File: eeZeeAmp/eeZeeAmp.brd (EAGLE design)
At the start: 21.3 x 13.7 mm, 11 parts, among them IC1 LM386

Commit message: Minor updates, added gerbers, zip
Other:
- board text added: "10"
- board text added: "104"
- board text added: "106"
- board text added: "1K"
- board text added: "220uF"
- board text added: "503"
- board text added: "LM386"
- board text added: "VOL"

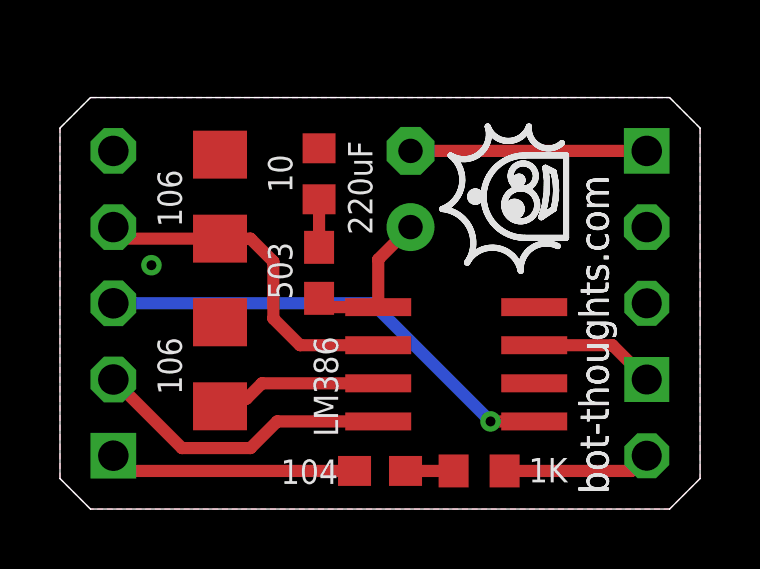
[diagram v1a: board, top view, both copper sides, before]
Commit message: Final version of silk
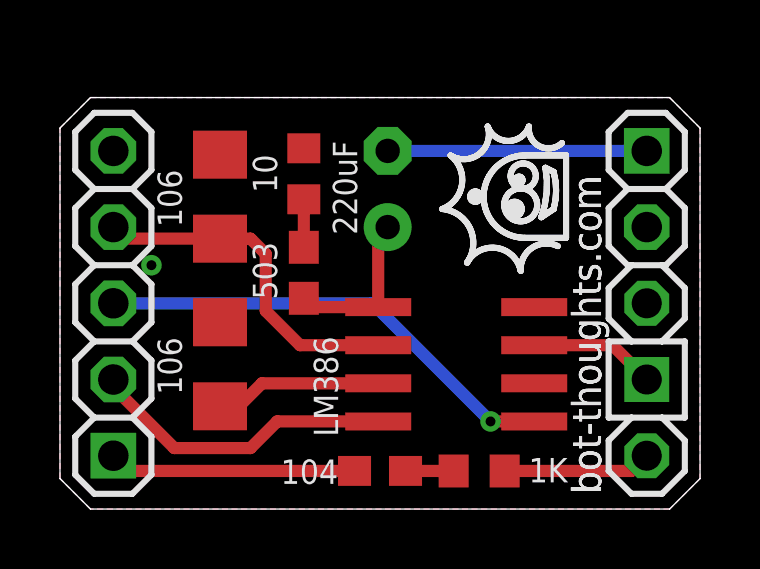
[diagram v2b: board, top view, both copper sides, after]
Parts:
- moved C1 0.76 mm to (10.9, 10.7)
- moved C3 0.51 mm to (8.13, 7.87)
- moved R1 0.51 mm to (8.13, 11.2)
- flipped JP1 to the top
- flipped JP2 to the top
- flipped R2 to the top
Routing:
- net SP+: track 7.87 -> 8.64 mm
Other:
- board text added: "1"
- board text added: "8"
- board text added: "GAIN"
- board text removed: "G1"
- board text removed: "G8"

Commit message: Fixed silk pin 1 on LM386, updated version #
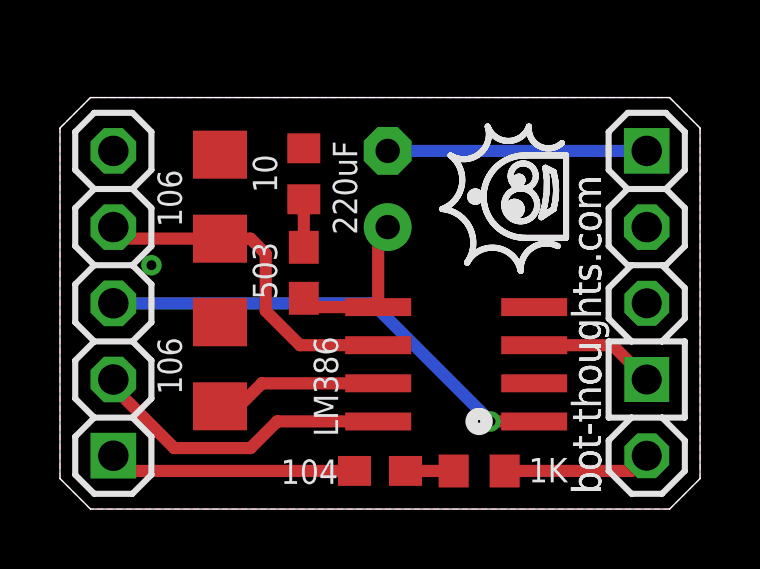
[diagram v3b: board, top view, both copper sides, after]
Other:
- board text added: "R0.2"
- board text removed: "R0.1"
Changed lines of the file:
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@@
 <layer number="49" name="Reference" color="7" fill="1" visible="no" active="yes"/>
 <layer number="50" name="dxf" color="7" fill="1" visible="no" active="no"/>
-<layer number="51" name="tDocu" color="7" fill="1" visible="no" active="yes"/>
+<layer number="51" name="tDocu" color="7" fill="1" visible="yes" active="yes"/>
 <layer number="52" name="bDocu" color="7" fill="1" visible="no" active="yes"/>
 <layer number="53" name="tPadExt" color="7" fill="1" visible="no" active="no"/>
@@
 <text x="18.288" y="8.89" size="1.27" layer="26" font="vector" ratio="12" rot="MR0">SP-</text>
 <text x="15.748" y="6.35" size="1.27" layer="26" font="vector" ratio="12" rot="MR0">eeZeeAmp</text>
-<text x="14.986" y="5.08" size="1.016" layer="26" font="vector" ratio="12" rot="MR0">R0.1</text>
+<text x="14.986" y="5.08" size="1.016" layer="26" font="vector" ratio="12" rot="MR0">R0.2</text>
 <text x="18.034" y="0.508" size="0.9652" layer="25" font="vector" ratio="12" rot="R90">bot-thoughts.com</text>
 <polygon width="0.254" layer="22">
@@
 <text x="18.288" y="8.89" size="1.27" layer="122" font="vector" ratio="16" rot="MR0">SP-</text>
 <text x="15.748" y="6.35" size="1.27" layer="122" font="vector" ratio="16" rot="MR0">eeZeeAmp</text>
-<text x="14.986" y="5.08" size="1.016" layer="122" font="vector" ratio="20" rot="MR0">R0.1</text>
+<text x="14.986" y="5.08" size="1.016" layer="122" font="vector" ratio="20" rot="MR0">R0.2</text>
 <text x="18.288" y="1.27" size="1.016" layer="122" font="vector" ratio="20" rot="MR0">+</text>
 <text x="18.288" y="6.35" size="1.016" layer="122" font="vector" ratio="20" rot="MR0">-</text>
@@
 <text x="15.621" y="0.889" size="0.8128" layer="121" font="vector" ratio="25">1K</text>
 <text x="17.272" y="5.842" size="1.27" layer="122" font="vector" ratio="16" rot="SMR270">VOL</text>
+<circle x="13.97" y="2.921" radius="0.254" width="0.4064" layer="21"/>
 </plain>
 <attributes>

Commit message: Narrowed by 0.1", complete redo of layout, text, accommodated larger 8mm output cap, fitted decoupling 0.1uF, located all gnd near to avoid loop, removed top ground pour
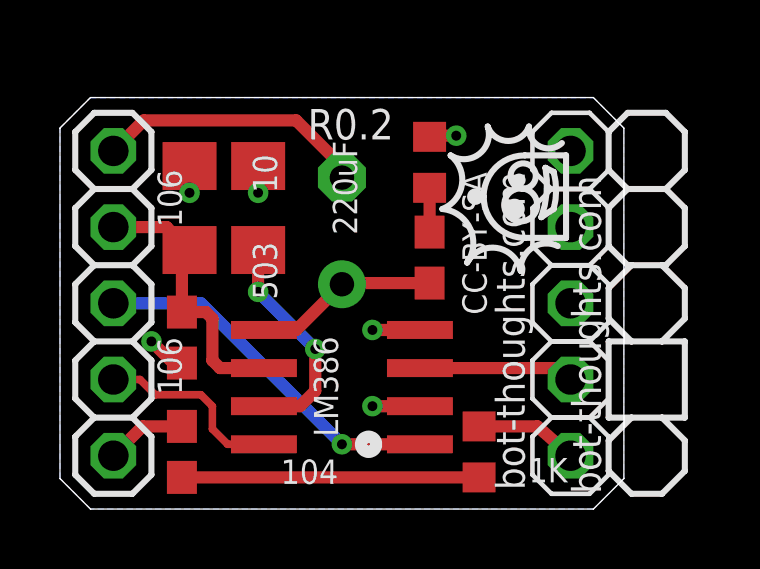
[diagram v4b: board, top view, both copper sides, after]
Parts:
- removed R2: VOL, bt:OFFBOARD_POT_3
- added C6: 104, rcl:C0603
- added JP10: GND, pinhead-2:1X01-S
- added JP3: 1, pinhead-2:1X01-S
- added JP4: VR-, pinhead-2:1X01-S
- added JP5: IN+, pinhead-2:1X01-S
- added JP6: V+, pinhead-2:1X01-S
- added JP7: SP+, pinhead-2:1X01-S
- added JP8: 8, pinhead-2:1X01-S
- added JP9: VR+, pinhead-2:1X01-S
- C1: device rcl:E2,5-6 -> rcl:E3,5-8
- JP1: value (none) -> GND; device pinhead-2:1X05-S -> pinhead-2:1X01-S
- JP2: value SPKR -> >; device pinhead-2:1X02-S -> pinhead-2:1X01-S
- moved JP1 16.1 mm to (17.0, 11.9), turned to 0 degrees
- moved JP2 6.84 mm to (17.0, 4.32), turned to 0 degrees
- moved C2 6.63 mm to (4.06, 1.91), turned to 270 degrees
- moved C5 5.36 mm to (6.60, 10.0)
- moved C3 4.22 mm to (12.3, 8.38)
- moved R1 4.21 mm to (12.3, 11.6)
- moved IC1 3.89 mm to (9.40, 4.06)
- moved C1 2.07 mm to (9.40, 9.27)
- moved C4 1.09 mm to (4.32, 10.0)
- moved R3 0.64 mm to (14.0, 1.91), turned to 270 degrees
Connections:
- net N$3 renamed 5
- net N$7 renamed 7
- removed net AUDIO: C2.1, JP1.1
- removed net G1: IC1.1, JP1.3
- removed net G8: IC1.8, JP1.2
- removed net N$1: IC1.3, R2.P$2
- removed net SP+: C1.-, JP2.1
- new net 1: IC1.1, JP3.1
- new net 3: IC1.3, JP2.1
- new net 8: IC1.8, JP8.1
- new net AUDIO_IN: C2.1, JP5.1
- new net SPEAKER: C1.-, JP7.1
- net GND: now also C6.2, JP1.1, JP10.1, JP4.1; no longer JP1.5, JP2.2, R2.P$1
- net N$8: now also JP9.1; no longer R2.P$3
- net VCC: now also C6.1, JP6.1; no longer JP1.4
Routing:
- net G1: track 15.7 -> 0.00 mm, vias 1 -> 0
- net 1: track 0.00 -> 12.2 mm, vias 0 -> 1
- net G8: track 10.3 -> 0.00 mm
- net SPEAKER: track 0.00 -> 9.05 mm
- net SP+: track 8.64 -> 0.00 mm
- net N$2: track 1.60 -> 9.91 mm
- net AUDIO: track 8.25 -> 0.00 mm
- net GND: track 0.00 -> 7.17 mm, vias 1 -> 6
- net 8: track 0.00 -> 6.36 mm
- net 3: track 0.00 -> 5.18 mm
- net N$1: track 4.22 -> 0.00 mm
- net AUDIO_IN: track 0.00 -> 2.69 mm
- net VCC: track 11.6 -> 9.36 mm
- net 7: track 5.59 -> 7.41 mm, vias 0 -> 2
- net N$8: track 4.95 -> 3.42 mm
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- removed copper zone on layer 1, net GND
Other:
- board size 21.3 x 13.7 mm -> 18.8 x 13.7 mm
- board text added: "CC-BY-SA"
